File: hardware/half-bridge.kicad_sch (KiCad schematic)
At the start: 12 parts, among them Q1 Q_NMOS_GSD, Q2 Q_NMOS_GSD

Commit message: half bridges
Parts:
- removed C14: 100n, symbol Device:C
- removed R6: 10, symbol Device:R
- removed R7, R8: 100k, symbol Device:R
- added C17: 2.2u, symbol Device:C
- added C18, C19: 1u, symbol Device:C
- added C20: 100n, symbol Device:C
- added D4: SS34, Diode_SMD:D_SMA, symbol Diode:SS34
- added J7: Phase_OUT, MountingHole:MountingHole_5.3mm_M5_DIN965_Pad, symbol Connector_Generic:Conn_01x01
- added Q1, Q3, Q4, Q6: AGM015N10LL, Package_TO_SOT_SMD:Infineon_PG-HSOF-8-1_ThermalVias, symbol Transistor_FET:Q_NMOS_GSD
- added R17: R, symbol Device:R
- added R19, R22: 1, symbol Device:R
- added TH1: 10k, symbol Device:Thermistor_NTC
- added U3: IRS21867S, Package_SO:SOIC-8_3.9x4.9mm_P1.27mm, symbol Driver_FET:IRS21867S
- added U4: INA240A2D, Package_SO:SOIC-8_3.9x4.9mm_P1.27mm, symbol Amplifier_Current:INA240A2D
- Q2: value Q_NMOS_GSD -> AGM015N10LL; footprint (none) -> Package_TO_SOT_SMD:Infineon_PG-HSOF-8-1_ThermalVias
- Q5: renamed from Q1; value Q_NMOS_GSD -> AGM015N10LL; footprint (none) -> Package_TO_SOT_SMD:Infineon_PG-HSOF-8-1_ThermalVias
- R20: renamed from R9; value 100k -> 56k
- R21: renamed from R5; value 10 -> 1
- R24: renamed from R10; footprint (none) -> Resistor_SMD:R_4020_10251Metric; LCSC (none) -> C558625
- renumbered R13 to R18, R11 to R23, R12 to R25
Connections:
- net GND: now also Q2.2 (S), C17.2, C18.2, Q4.2 (S), Q6.2 (S), TH1.2, U3.4 (COM), U4.2 (GND), U4.4 (GND), U4.7 (REF1); no longer Q2.3 (D)
- net VS: now also Q1.3 (D), Q3.3 (D)
- net at Q2.1 (G): now also Q4.1 (G), Q6.1 (G), R22.2
- net at Q5.2 (S), R20.2, R23.2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: now also Q2.3 (D), Q1.2 (S), Q3.2 (S), Q4.3 (D), Q6.3 (D), R19.2; no longer Q2.2 (S)
- net Phase_V_sense: now reaches R18.2, R20.1
- net at R25.1: now also C20.1, U4.1 (-)
- net at Q5.1 (G), R21.2: now also Q1.1 (G), Q3.1 (G)
- net at R23.1: now also C20.2, U4.8 (+)
- net High_Side_Gate: no longer names the net of R21.1
- net High_Side_Gate: now also U3.7 (HO)
- net LOAD: no longer names the net of R24.1, R25.2
- net LOAD: now also J7.1 (Pin_1)
- new net: R22.1, U3.5 (LO)
- new net: C19.2, R19.1, U3.6 (VS)
- new net: C19.1, D4.1 (K), U3.8 (VB)
- new net +12V: C18.1, D4.2 (A), U3.1 (VCC)
- new net +3.3V: R17.1, U4.3 (REF2), U4.6 (V+)
- new net Current_sense: U4.5
- new net HIGH: U3.2 (HIN)
- new net LOW: U3.3 (LIN)
- new net TEMP: C17.1, R17.2, TH1.1
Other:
- moved on the sheet: Q5, R18, R20, R21, R23, R24, R25

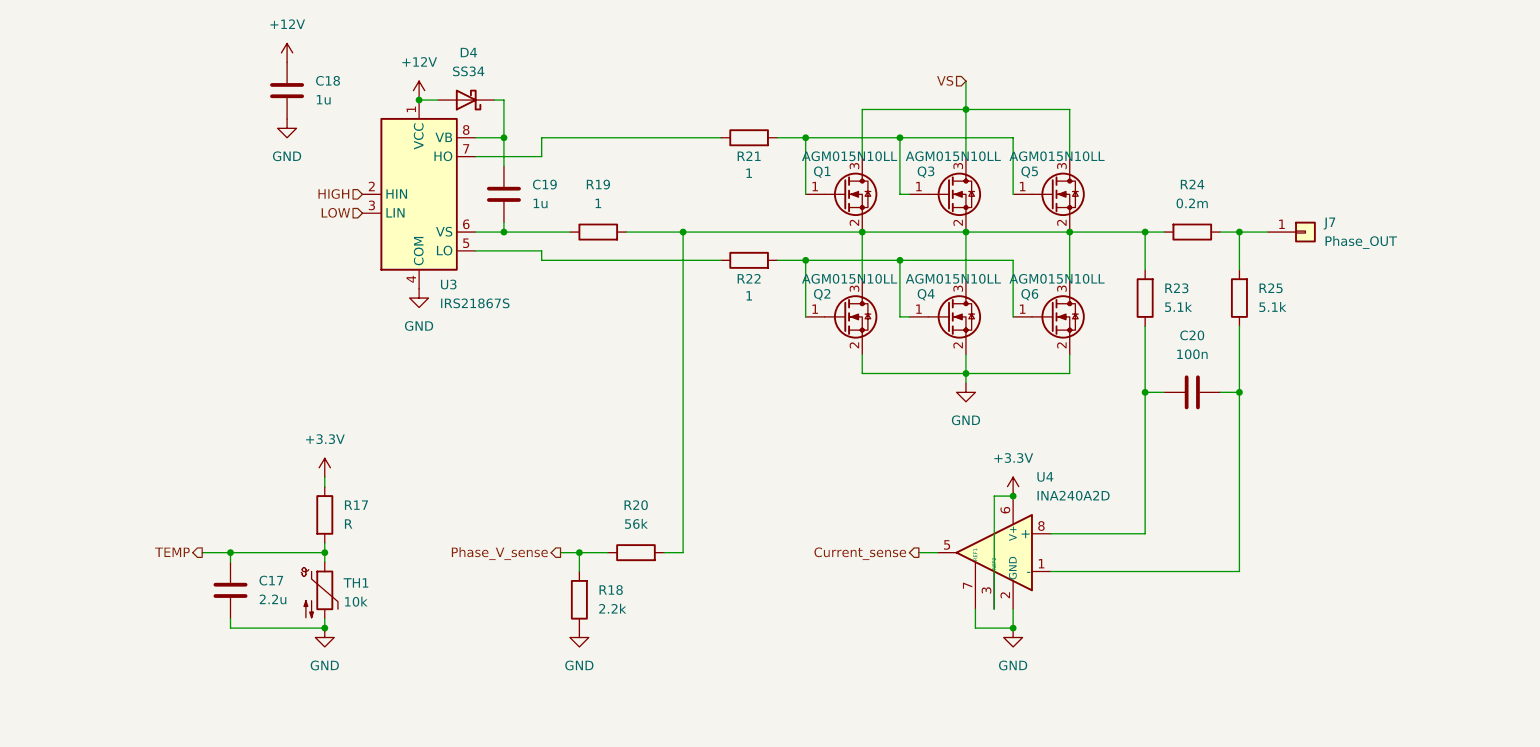
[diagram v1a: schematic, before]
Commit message: phase capacitors
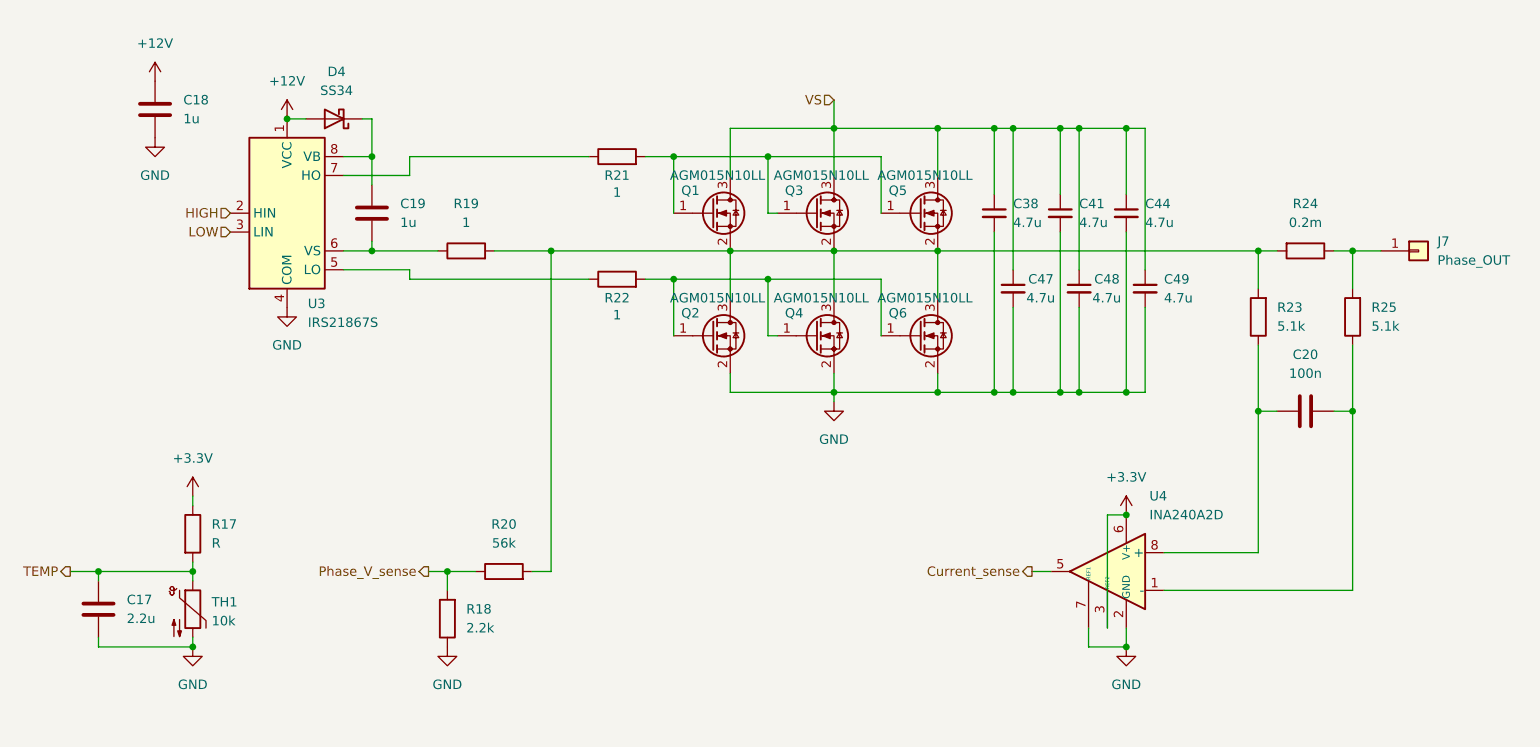
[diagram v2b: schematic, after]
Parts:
- added C38, C41, C44, C47, C48, C49: 4.7u, Capacitor_SMD:C_1210_3225Metric, symbol Device:C_Small
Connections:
- net GND: now also C38.2, C41.2, C44.2, C47.2, C48.2, C49.2
- net VS: now also C38.1, C41.1, C44.1, C47.1, C48.1, C49.1
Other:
- moved on the sheet: C17, C18, C19, C20, D4, J7, Q1, Q2, Q3, Q4, Q5, Q6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

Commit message: Placement study
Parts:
- removed C17: 2.2u, symbol Device:C
- removed C38, C41, C47, C48: 4.7u, Capacitor_SMD:C_1210_3225Metric, symbol Device:C_Small
- removed D4: SS34, Diode_SMD:D_SMA, symbol Diode:SS34
- removed Q1, Q2, Q3, Q4: AGM015N10LL, Package_TO_SOT_SMD:Infineon_PG-HSOF-8-1_ThermalVias, symbol Transistor_FET:Q_NMOS_GSD
- removed R17: R, symbol Device:R
- removed TH1: 10k, symbol Device:Thermistor_NTC
- added D4: PMEG2010EH, Diode_SMD:D_SOD-123F, symbol Diode:PMEG2010EH
- C18: footprint (none) -> Capacitor_SMD:C_1206_3216Metric
- C19: footprint (none) -> Capacitor_SMD:C_0805_2012Metric
- C20: footprint (none) -> Capacitor_SMD:C_0402_1005Metric
- C49: footprint Capacitor_SMD:C_1210_3225Metric -> Capacitor_SMD:C_3640_9110Metric
- R18: footprint (none) -> Resistor_SMD:R_0402_1005Metric
- R19, R21, R22: footprint (none) -> Resistor_SMD:R_0805_2012Metric
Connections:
- net +12V: now also D4.2 (A)
- net Center: now reaches Q5.2 (S), Q6.3 (D), R19.2, R20.2
- net Center: now also R24.1, R25.2; no longer R23.2, R24.2
- net LS: now reaches R22.1, U3.5 (LO)
- net HS: now reaches R21.1, U3.7 (HO)
- net at C19.1, U3.8 (VB): now also D4.1 (K)
- net Phase_V_sense renamed Phase_V
- new net: J7.1 (Pin_1), R23.2, R24.2
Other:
- moved on the sheet: C18, C19, C20, C44, C49, J7, Q5, Q6, R18, R19, R20, R21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

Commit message: Power Layout
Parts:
- C49: footprint Capacitor_SMD:C_3640_9110Metric -> Capacitor_SMD:C_1210_3225Metric
- R24: footprint Resistor_SMD:R_4020_10251Metric -> greenmobi:R_3920
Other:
- title: (none) -> GreenMobi Drive
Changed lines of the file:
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@@
 	(generator_version "9.0")
 	(paper "A4")
+	(title_block
+		(title "GreenMobi Drive")
+		(date "2025-07-02")
+		(rev "0.1")
+	)
 	(junction
 		(at 129.54 132.08)
@@
 			)
 		)
-		(property "Footprint" "Resistor_SMD:R_4020_10251Metric"
+		(property "Footprint" "greenmobi:R_3920"
 			(at 153.67 79.502 90)
 			(effects
@@
 			)
 		)
-		(property "Footprint" "Capacitor_SMD:C_3640_9110Metric"
+		(property "Footprint" "Capacitor_SMD:C_1210_3225Metric"
 			(at 199.39 80.01 0)
 			(effects

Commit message: Layout
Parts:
- added C17: 100n, Capacitor_SMD:C_0402_1005Metric, symbol Device:C_Small
- R24: footprint greenmobi:R_3920 -> Resistor_SMD:R_2512_6332Metric; LCSC C558625 -> C4944115
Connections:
- net +3.3V: now also C17.1
- net GND: now also C17.2
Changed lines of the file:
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@@
+	)
+	(symbol
+		(lib_id "Device:C_Small")
+		(at 106.68 134.62 0)
+		(unit 1)
+		(exclude_from_sim no)
+		(in_bom yes)
+		(on_board yes)
+		(dnp no)
+		(fields_autoplaced yes)
+		(property "Reference" "C17"
+			(at 109.22 133.3562 0)
+			(effects
+				(font
+					(size 1.27 1.27)
+				)
+				(justify left)
+			)
+		)
+		(property "Value" "100n"
+			(at 109.22 135.8962 0)
+			(effects
+				(font
+					(size 1.27 1.27)
+				)
+				(justify left)
+			)
+		)
+		(property "Footprint" "Capacitor_SMD:C_0402_1005Metric"
+			(at 106.68 134.62 0)
+			(effects
+				(font
+					(size 1.27 1.27)
+				)
+				(hide yes)
+			)
+		)
+		(property "Datasheet" "~"
+			(at 106.68 134.62 0)
+			(effects
+				(font
+					(size 1.27 1.27)
+				)
+				(hide yes)
+			)
+		)
+		(property "Description" "Unpolarized capacitor, small symbol"
+			(at 106.68 134.62 0)
+			(effects
+				(font
+					(size 1.27 1.27)
+				)
+				(hide yes)
+			)
+		)
+		(pin "2"
+		)
+		(pin "1"
+		)
+		(instances
+			(project ""
+				(path "/a12b77e7-bd0f-4a70-9ba2-19a87ce48819/4a5d7eb9-ddee-45d4-92b5-174bd9809dbc"
+					(reference "C38")
+					(unit 1)
+				)
+				(path "/a12b77e7-bd0f-4a70-9ba2-19a87ce48819/caef660a-9a2f-49e8-a393-a85edb78ce64"
+					(reference "C25")
+					(unit 1)
+				)
+				(path "/a12b77e7-bd0f-4a70-9ba2-19a87ce48819/cd601179-baef-4e34-b5da-beea03762ae5"
+					(reference "C17")
+					(unit 1)
+				)
+			)
+		)
 	)
 	(symbol
@@
 			)
 		)
-		(property "Footprint" "greenmobi:R_3920"
+		(property "Footprint" "Resistor_SMD:R_2512_6332Metric"
 			(at 153.67 79.502 90)
 			(effects
@@
 			)
 		)
-		(property "LCSC" "C558625"
+		(property "LCSC" "C4944115"
 			(at 153.67 81.28 90)
 			(effects
@@
 				(path "/a12b77e7-bd0f-4a70-9ba2-19a87ce48819/cd601179-baef-4e34-b5da-beea03762ae5"
 					(reference "R24")
+					(unit 1)
+				)
+			)
+		)
+	)
+	(symbol
+		(lib_id "power:GND")
+		(at 106.68 137.16 0)
+		(unit 1)
+		(exclude_from_sim no)
+		(in_bom yes)
+		(on_board yes)
+		(dnp no)
+		(fields_autoplaced yes)
+		(property "Reference" "#PWR066"
+			(at 106.68 143.51 0)
+			(effects
+				(font
+					(size 1.27 1.27)
+				)
+				(hide yes)
+			)
+		)
+		(property "Value" "GND"
+			(at 106.68 142.24 0)
+			(effects
+				(font
+					(size 1.27 1.27)
+				)
+			)
+		)
+		(property "Footprint" ""
+			(at 106.68 137.16 0)
+			(effects
+				(font
+					(size 1.27 1.27)
+				)
+				(hide yes)
+			)
+		)
+		(property "Datasheet" ""
+			(at 106.68 137.16 0)
+			(effects
+				(font
+					(size 1.27 1.27)
+				)
+				(hide yes)
+			)
+		)
+		(property "Description" "Power symbol creates a global label with name \"GND\" , ground"
+			(at 106.68 137.16 0)
+			(effects
+				(font
+					(size 1.27 1.27)
+				)
+				(hide yes)
+			)
+		)
+		(pin "1"
+		)
+		(instances
+			(project "greenmobi-drive"
+				(path "/a12b77e7-bd0f-4a70-9ba2-19a87ce48819/4a5d7eb9-ddee-45d4-92b5-174bd9809dbc"
+					(reference "#PWR084")
+					(unit 1)
+				)
+				(path "/a12b77e7-bd0f-4a70-9ba2-19a87ce48819/caef660a-9a2f-49e8-a393-a85edb78ce64"
+					(reference "#PWR083")
+					(unit 1)
+				)
+				(path "/a12b77e7-bd0f-4a70-9ba2-19a87ce48819/cd601179-baef-4e34-b5da-beea03762ae5"
+					(reference "#PWR066")
 					(unit 1)
 				)
@@
 					(unit 1)
 				)
+			)
+		)
+	)
+	(symbol
+		(lib_id "power:+3.3V")
+		(at 106.68 132.08 0)
+		(unit 1)
+		(exclude_from_sim no)
+		(in_bom yes)
+		(on_board yes)
+		(dnp no)
+		(fields_autoplaced yes)
+		(property "Reference" "#PWR045"
+			(at 106.68 135.89 0)
+			(effects
+				(font
+					(size 1.27 1.27)
+				)
+				(hide yes)
+			)
+		)
+		(property "Value" "+3.3V"
+			(at 106.68 127 0)
+			(effects
+				(font
+					(size 1.27 1.27)
+				)
+			)
+		)
+		(property "Footprint" ""
+			(at 106.68 132.08 0)
+			(effects
+				(font
+					(size 1.27 1.27)
+				)
+				(hide yes)
+			)
+		)
+		(property "Datasheet" ""
+			(at 106.68 132.08 0)
+			(effects
+				(font
+					(size 1.27 1.27)
+				)
+				(hide yes)
+			)
+		)
+		(property "Description" "Power symbol creates a global label with name \"+3.3V\""
+			(at 106.68 132.08 0)
+			(effects
+				(font
+					(size 1.27 1.27)
+				)
+				(hide yes)
+			)
+		)
+		(pin "1"
+		)
+		(instances
+			(project "greenmobi-drive"
+				(path "/a12b77e7-bd0f-4a70-9ba2-19a87ce48819/4a5d7eb9-ddee-45d4-92b5-174bd9809dbc"
+					(reference "#PWR065")
+					(unit 1)
+				)
+				(path "/a12b77e7-bd0f-4a70-9ba2-19a87ce48819/caef660a-9a2f-49e8-a393-a85edb78ce64"
+					(reference "#PWR046")
+					(unit 1)
+				)
+				(path "/a12b77e7-bd0f-4a70-9ba2-19a87ce48819/cd601179-baef-4e34-b5da-beea03762ae5"
+					(reference "#PWR045")
+					(unit 1)
+				)
